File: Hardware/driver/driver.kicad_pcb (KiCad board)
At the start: 4 copper layers, 128.1 x 184.5 mm, 168 parts, among them J201 Conn_02x10_Odd_Even, J301 1017526, J401 TBP02R2W-381-03BE, J402 Conn_01x02_Male, J501 Conn_Coaxial, J601 Screw_Terminal_01x02, K601 EC2-5TNU, M201 Fan_4pin, Q201 MMBT3904, Q202 PN2222A, Q301 IXTH80N075L2, Q302 IXTH80N075L2, Q601 MMBT3904, Q602 MMBT3904, U101 ICL7660, U102 DS2482-100, U103 PI4IOE5V9536, U201 AT24CS32-SSHM, U202 NCP716BCSN330T1G, U203 ADUM1250, U204 FODM217B, U205 FODM217B, U206 EMC2101-R, U301 MCP3421A2T-ECH, U302 OPA2388, U303 DAC60501Z, U304 LM431SC, U305 MCP3421A3T-ECH, U306 OPA2388, U307 DAC60501Z, U308 LM431SC, U309 DS18B20, U310 DS18B20, U501 74LVC1G17, U502 FODM217B, U601 MCP3421A1T-ECH, U602 OPA277

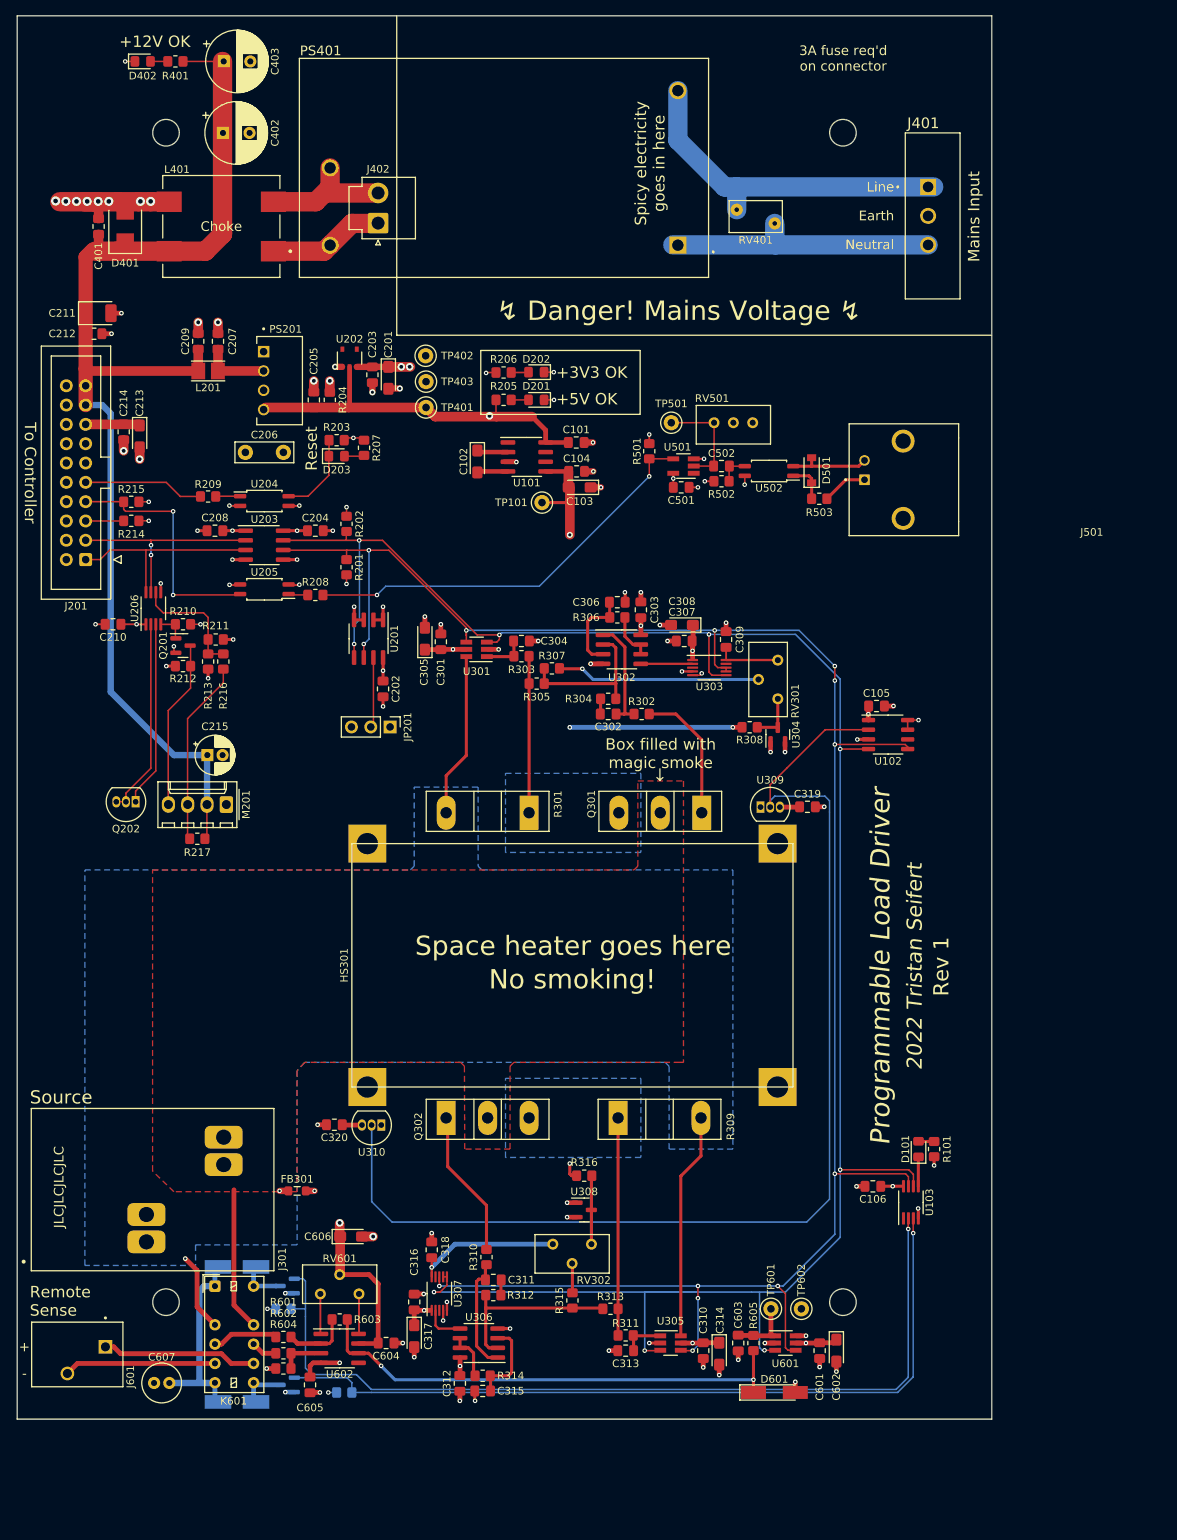
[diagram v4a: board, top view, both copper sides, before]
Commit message: Driver input protection; heatsink footprint tweaks
- Updated the footprint for the heatsink on the driver board to include
  a 3D model. Also fixed it… the distances were kind of out of whack and
  it would never have really fit

- Added a reverse polarity protection diode to the input; it gets its
  own cute little heatsink

- Minor movement to better accomodate a fan. A 20mm fan will likely
  interfere with the input connector (it might be worth switching to a
  different kind, or just soldering the connections altogether: spade
  terminals seem like a good choice for high current) and be very tight
  against the input diode's heatsink. We'll try with a 10mm fan and see
  if that's enough airflow.
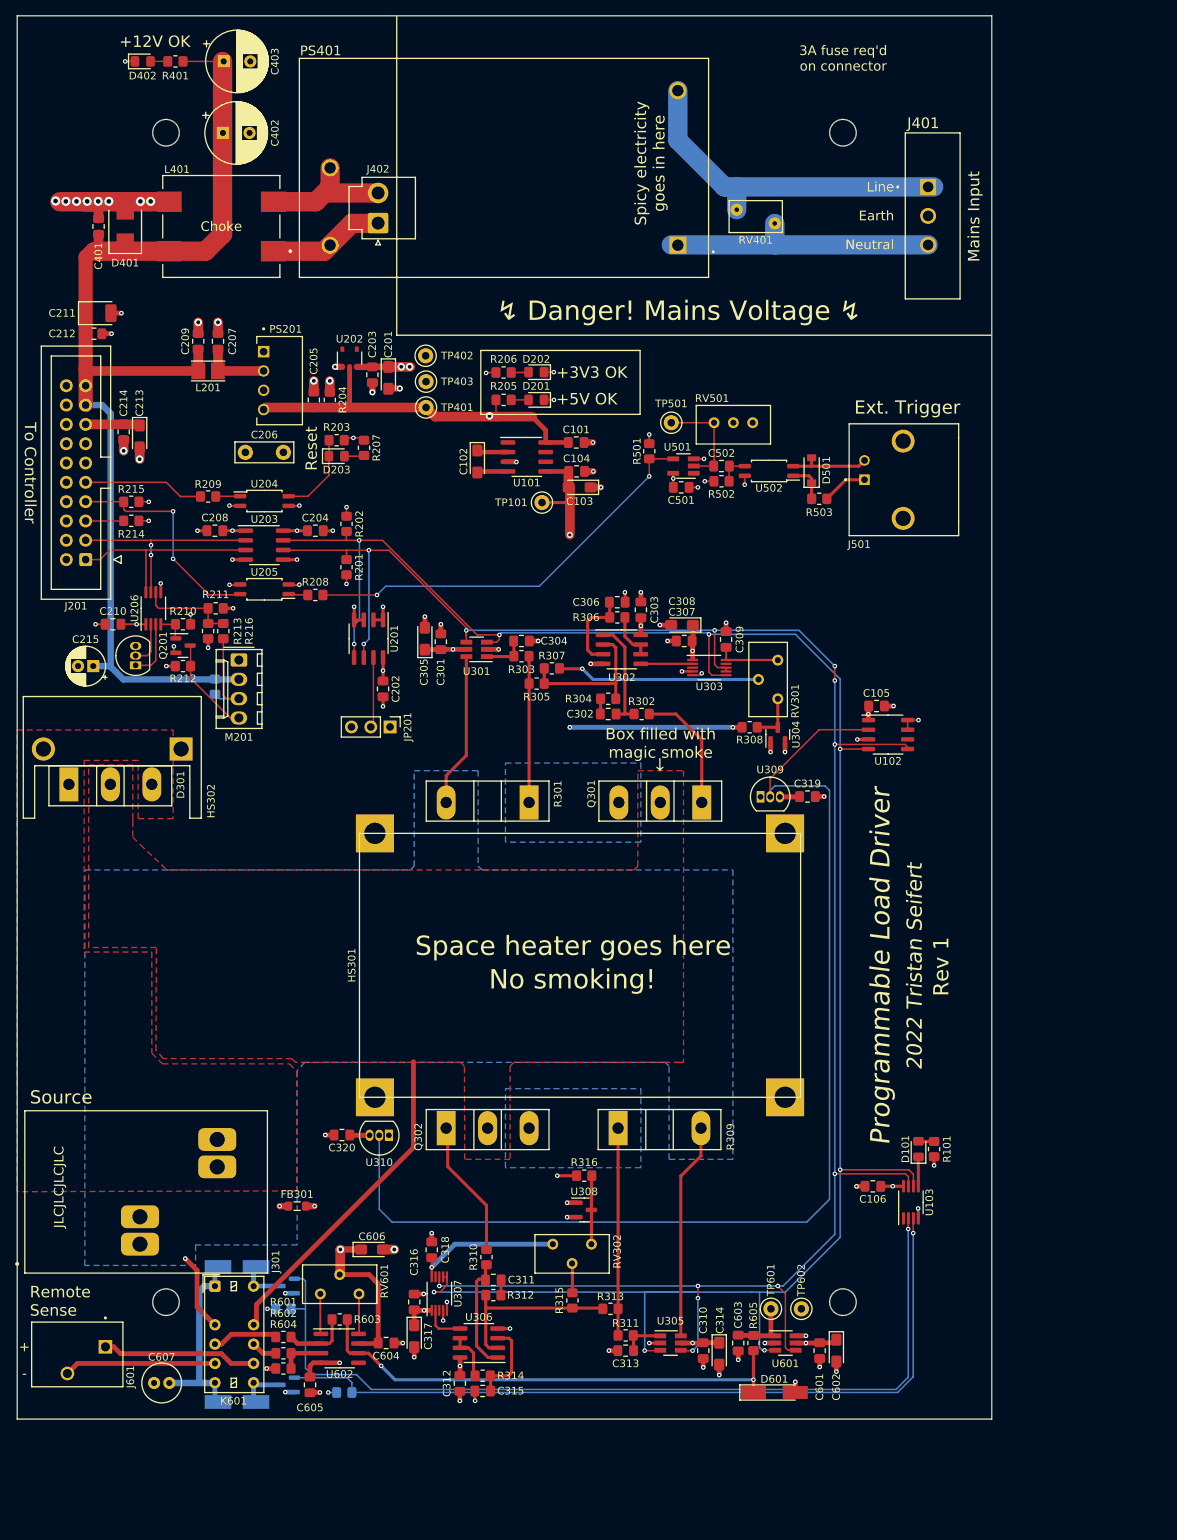
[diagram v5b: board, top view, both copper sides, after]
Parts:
- added D301: DSA120C150QB, Package_TO_SOT_THT:TO-247-3_Vertical, F.Cu at (26.8, 121.0)
- added HS302: WV-T247-101E, programmable-load:Ohmite-WA-T247-101E-MFG, F.Cu at (32.5, 117.5)
- R217: moved to B.Cu
- moved R217 20.1 mm to (46.0, 108.2), turned to 90 degrees
- moved M201 19.1 mm to (49.1, 104.7), turned to -90 degrees
- moved C215 19.0 mm to (30.0, 105.5), turned to 180 degrees
- moved Q202 17.9 mm to (35.6, 105.4), turned to 90 degrees
- moved R211 4.10 mm to (46.1, 97.9)
- moved R213 4.00 mm to (45.1, 100.9)
- moved R216 4.00 mm to (47.1, 100.9)
- moved C606 3.23 mm to (66.7, 182.2)
- moved FB301 2.00 mm to (56.8, 176.5)
- moved C320 1.68 mm to (62.7, 167.2)
- moved U310 1.68 mm to (68.9, 167.2)
- moved U309 1.35 mm to (117.7, 122.7)
- moved C319 1.35 mm to (123.9, 122.7)
- moved Q301 1.35 mm to (110.0, 123.4)
- moved Q302 1.35 mm to (76.4, 166.2)
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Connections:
- J301 pad 2: VBUS -> /Input Stage/VBUS_IN
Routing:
- net VBUS: track 18.8 -> 43.3 mm
- net /External Interface/TEMP_DP: track 26.0 -> 7.10 mm
- net /External Interface/TEMP_DN: track 24.4 -> 7.68 mm
- net Net-(M201-Pad3): track 24.4 -> 13.1 mm
- net +12VA: track 155.9 -> 145.2 mm
- net Net-(M201-Pad4): track 22.1 -> 12.8 mm
- net /External Interface/FAN_TACH: track 16.1 -> 12.7 mm
- net /External Interface/~{EXT_TRIG}: track 32.4 -> 29.6 mm
- net +5V: track 233.5 -> 234.9 mm
- net Net-(Q302-Pad1): track 19.5 -> 18.1 mm
- net /1WIRE: track 153.0 -> 151.7 mm
- added copper zone on F.Cu, net /Input Stage/VBUS_IN
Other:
- board text added: "Ext. Trigger"

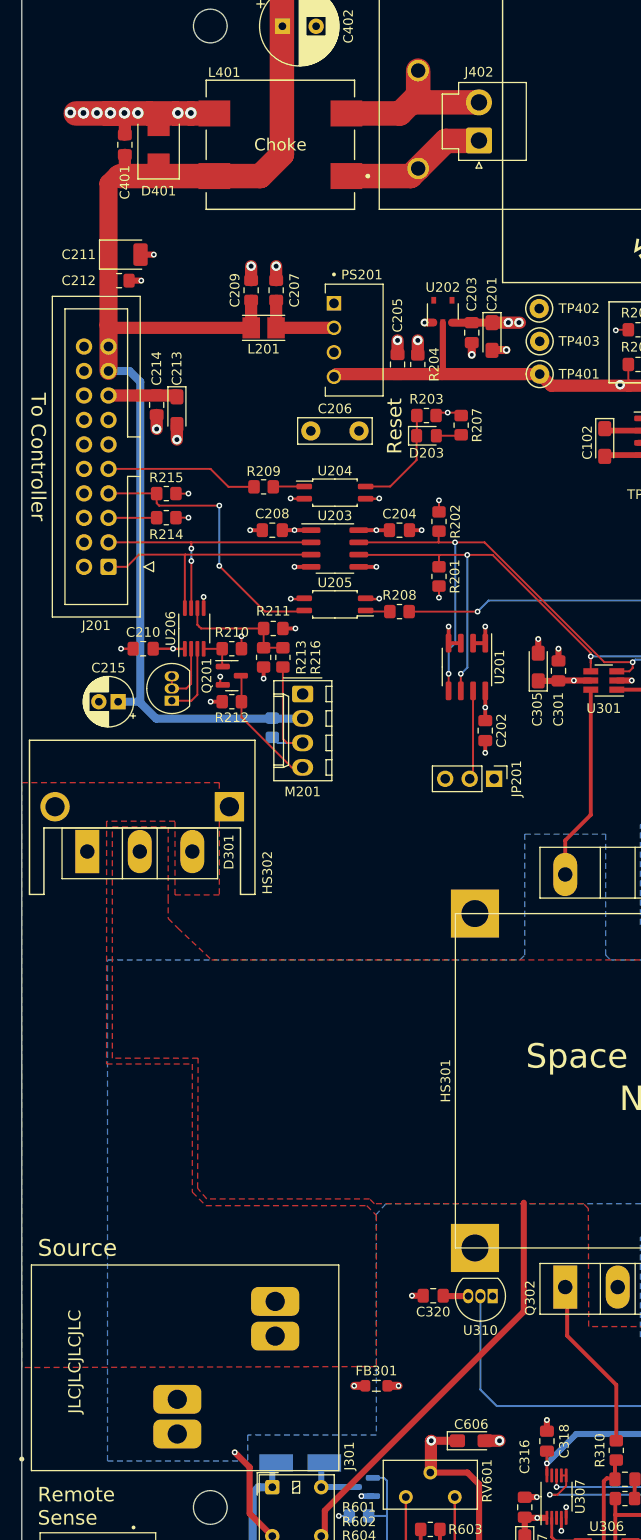
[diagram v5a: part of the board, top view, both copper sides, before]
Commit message: Replaced load input connector
- Switched out the screw terminal for a pair of PCB mount studs, which
  then accept the wires from the front panel (with crimped hook or loop
  ferrules) and an associated nut.

  This gives way more clearance for a fan so hopefully a big high
  velocity one can fit.

- Moved input protection diodes up some more
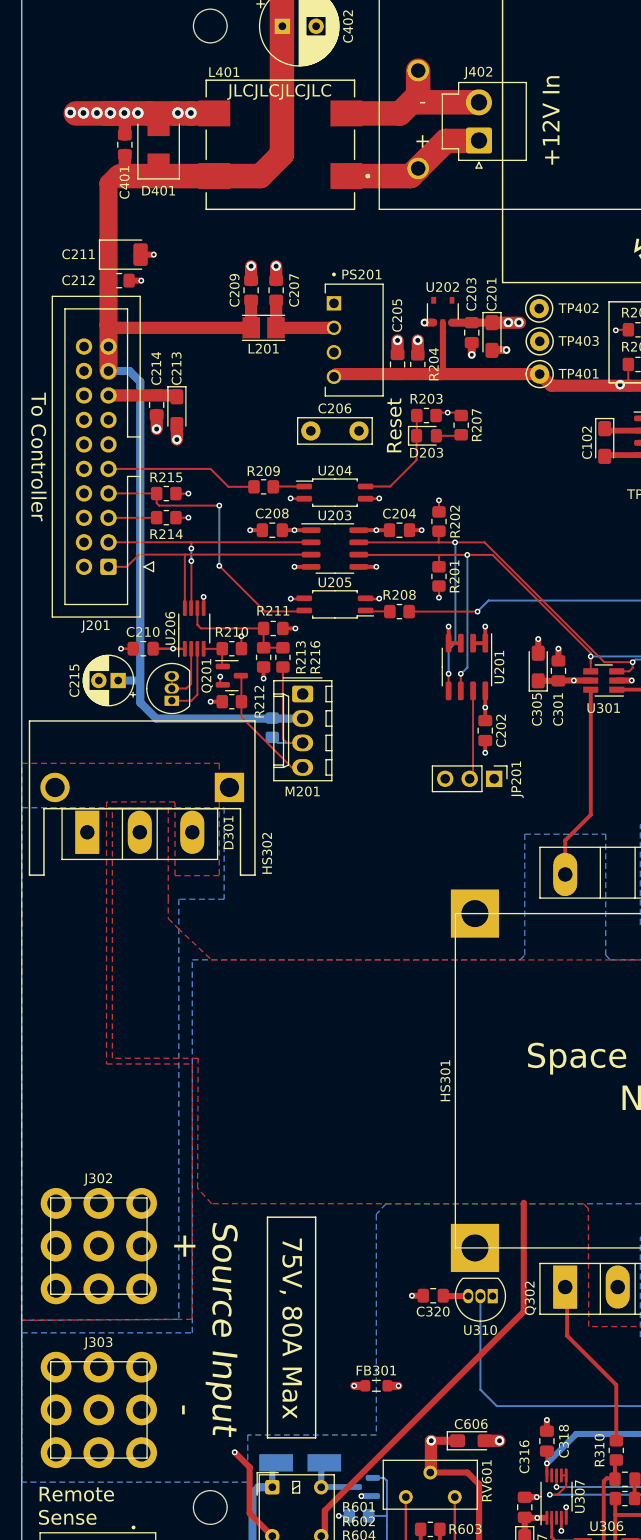
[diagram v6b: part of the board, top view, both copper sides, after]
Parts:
- removed J301: 1017526, programmable-load:Phoenix-TDPT-2,1017526
- added J302: Würth 74651194R, programmable-load:WE-74651194, F.Cu at (28.0, 162.0)
- added J303: Würth 74651194R, programmable-load:WE-74651194, F.Cu at (28.0, 179.0)
- moved C215 2.20 mm to (30.0, 103.3)
- moved D301 2.00 mm to (26.8, 119.0)
- moved HS302 2.00 mm to (32.5, 115.5)
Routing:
- added copper zone on B.Cu, net /Input Stage/VBUS_IN
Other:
- board text added: "+12V In"
- board text added: "75V, 80A Max"
- board text added: "Source Input"
- board text removed: "Source"

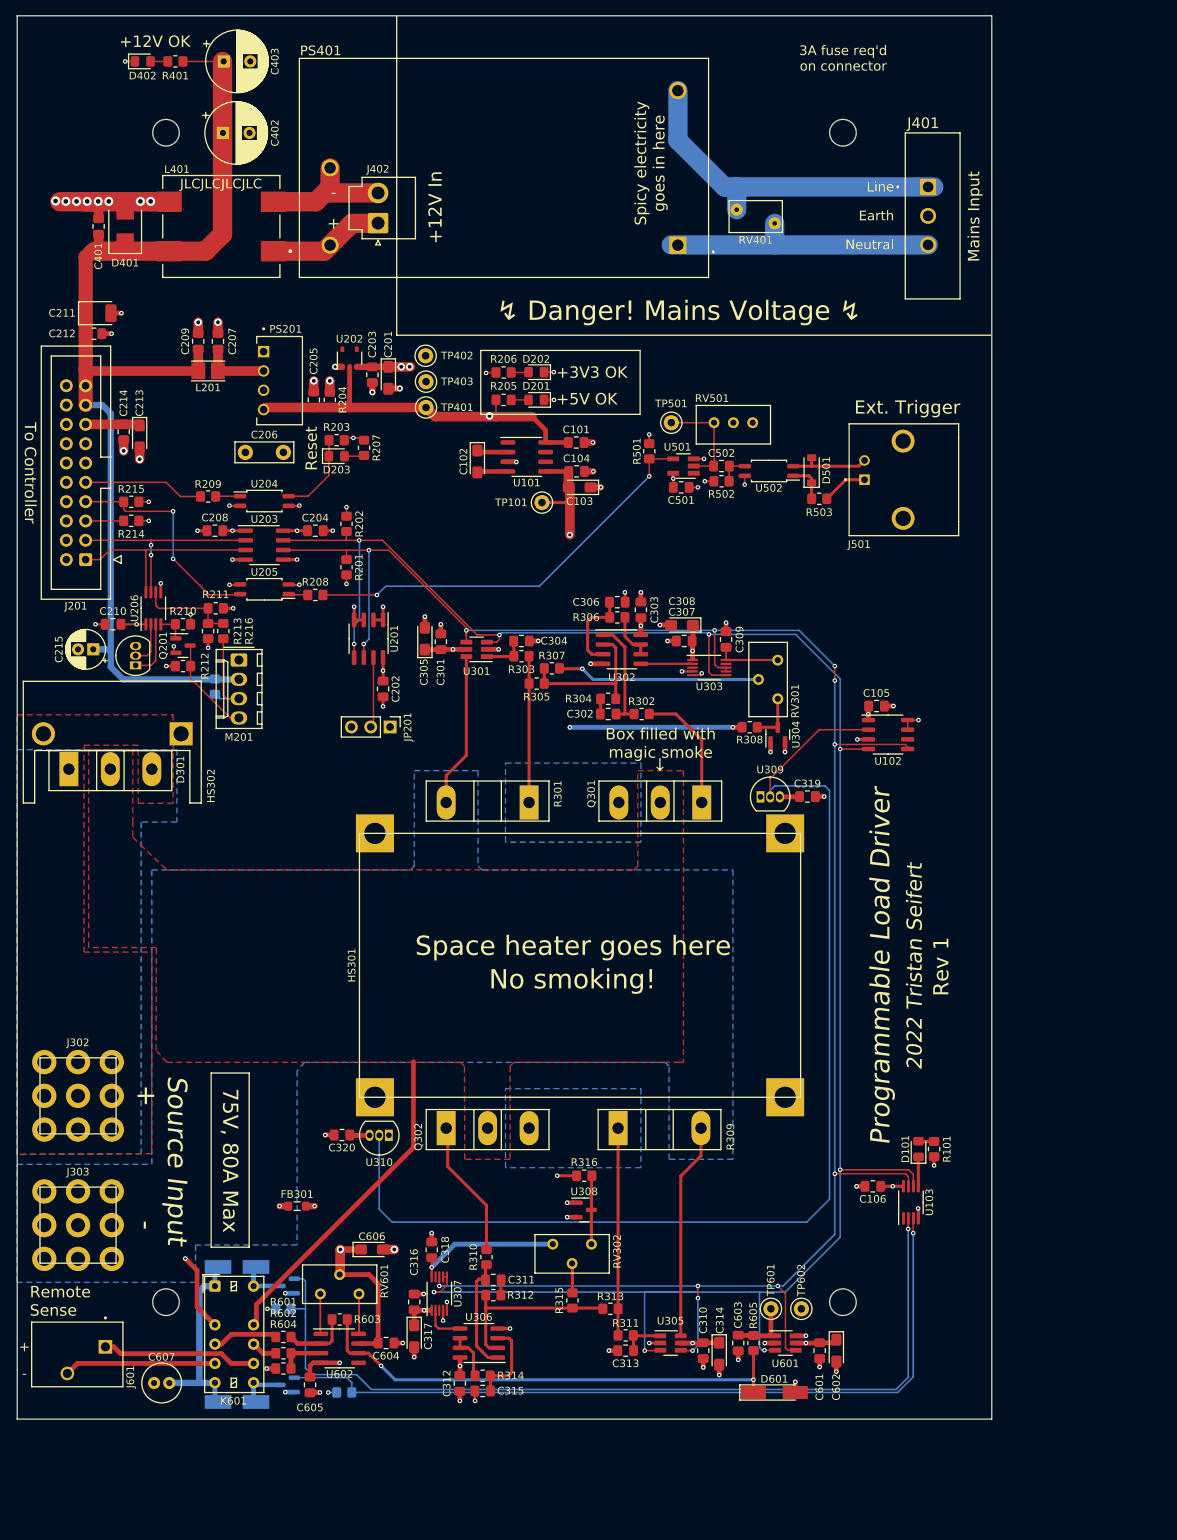
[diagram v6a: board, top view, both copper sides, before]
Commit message: Added some more protection to driver input
- Placed an overvoltage protection diode (TVS) at the input of the load
  driver board, and moved some more stuff around in preparation for
  manufacturing
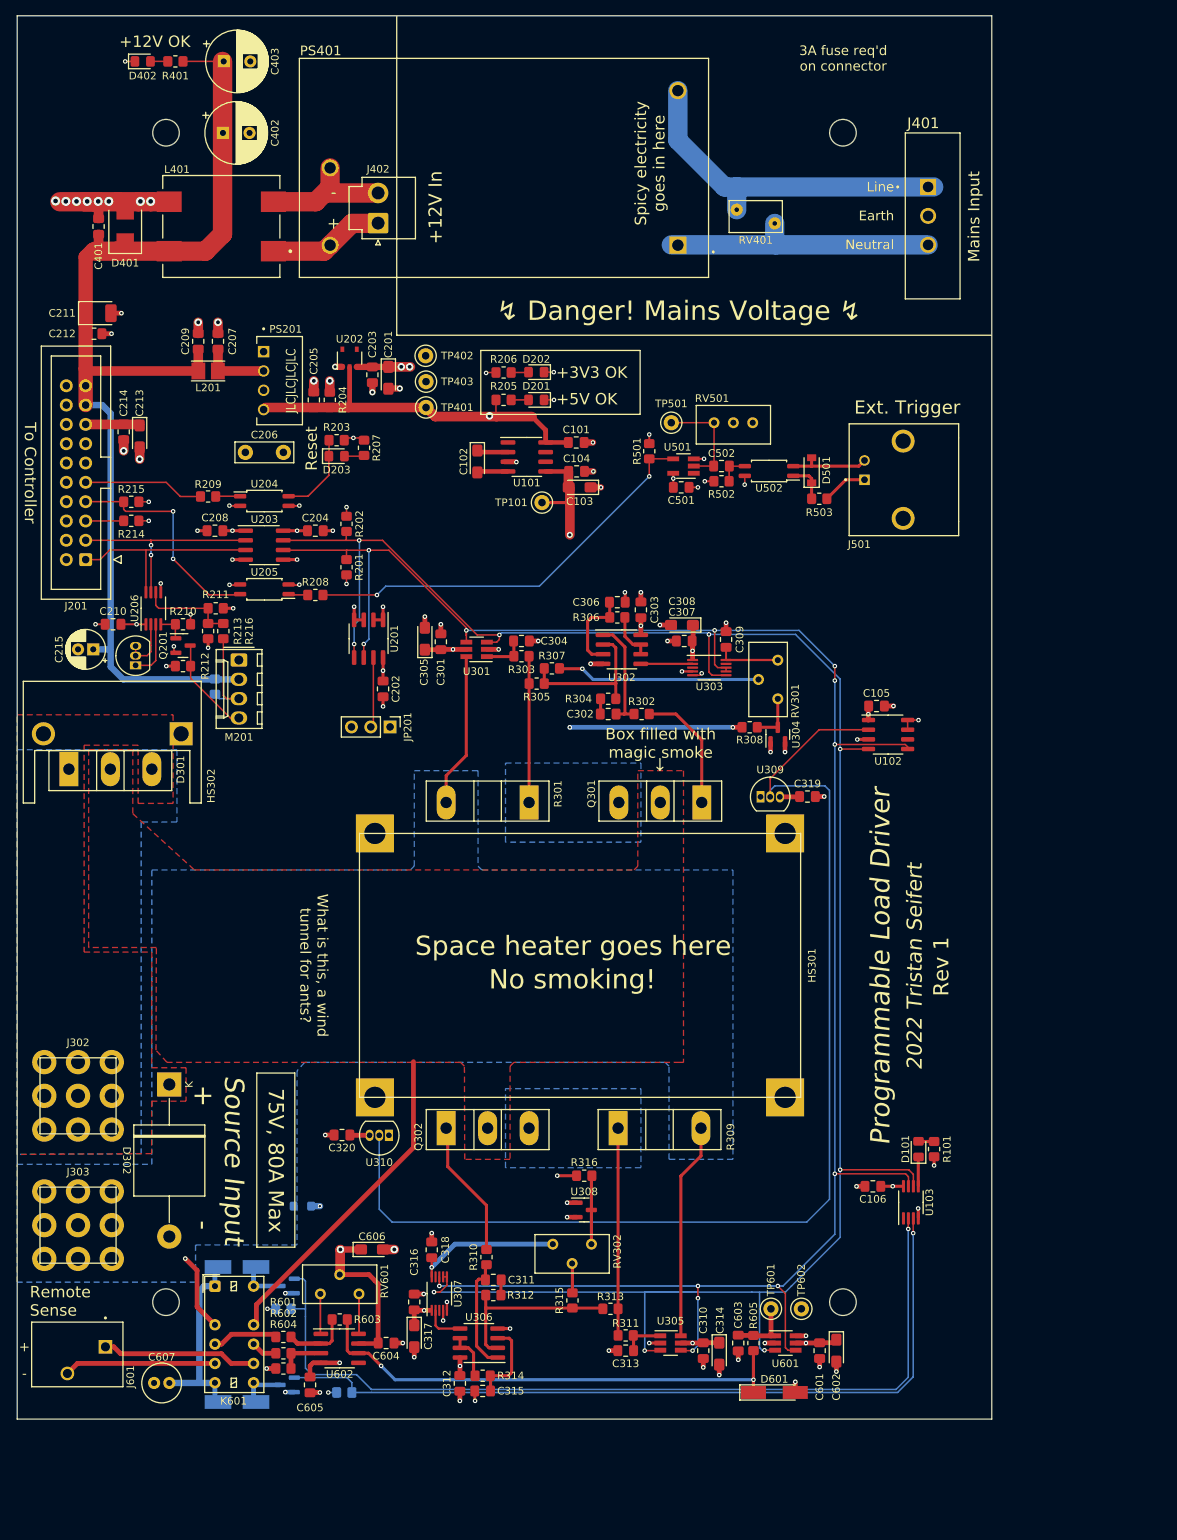
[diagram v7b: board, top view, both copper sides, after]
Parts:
- added D302: 5KP78A, Diode_THT:D_P600_R-6_P20.00mm_Horizontal, F.Cu at (40.0, 160.5)
- FB301: moved to B.Cu
- moved FB301 0.70 mm to (57.5, 176.5)
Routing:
- net GNDPWR: track 62.8 -> 61.7 mm, vias 2 -> 1
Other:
- board text added: "What is this, a wind tunnel for ants?"
